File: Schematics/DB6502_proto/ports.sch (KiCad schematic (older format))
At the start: 12 parts, among them J1 System Bus, J2 Controls, J4 I/O Bus

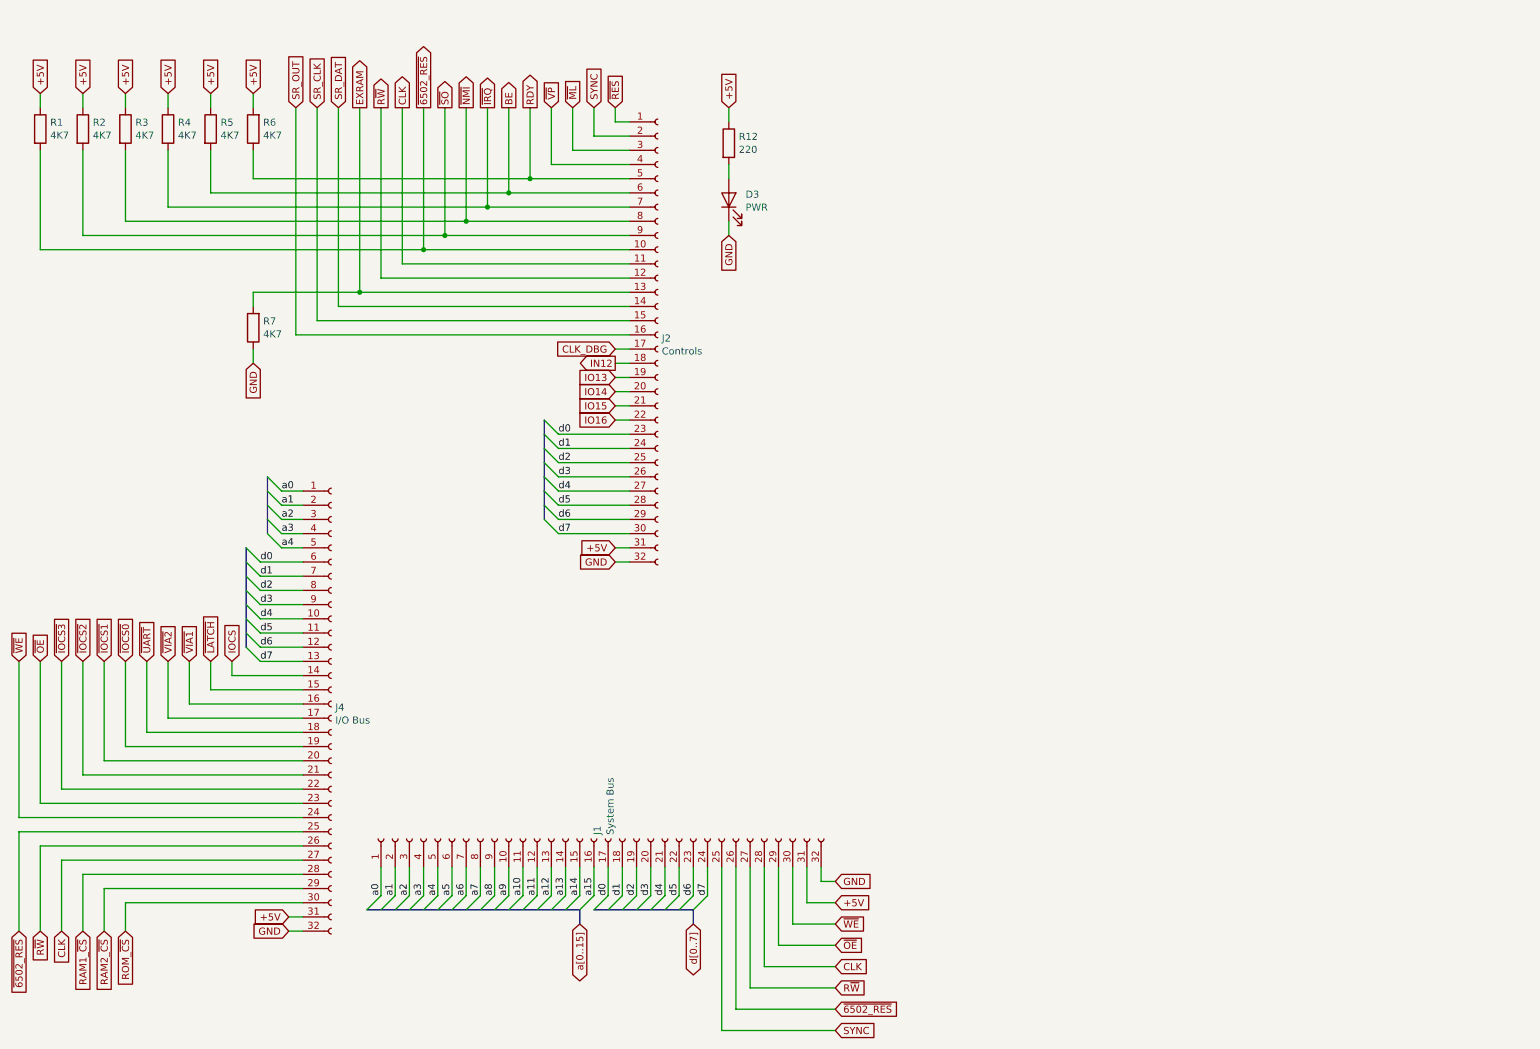
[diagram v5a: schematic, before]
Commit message: Implemented wait state generator, cleaned up schematic
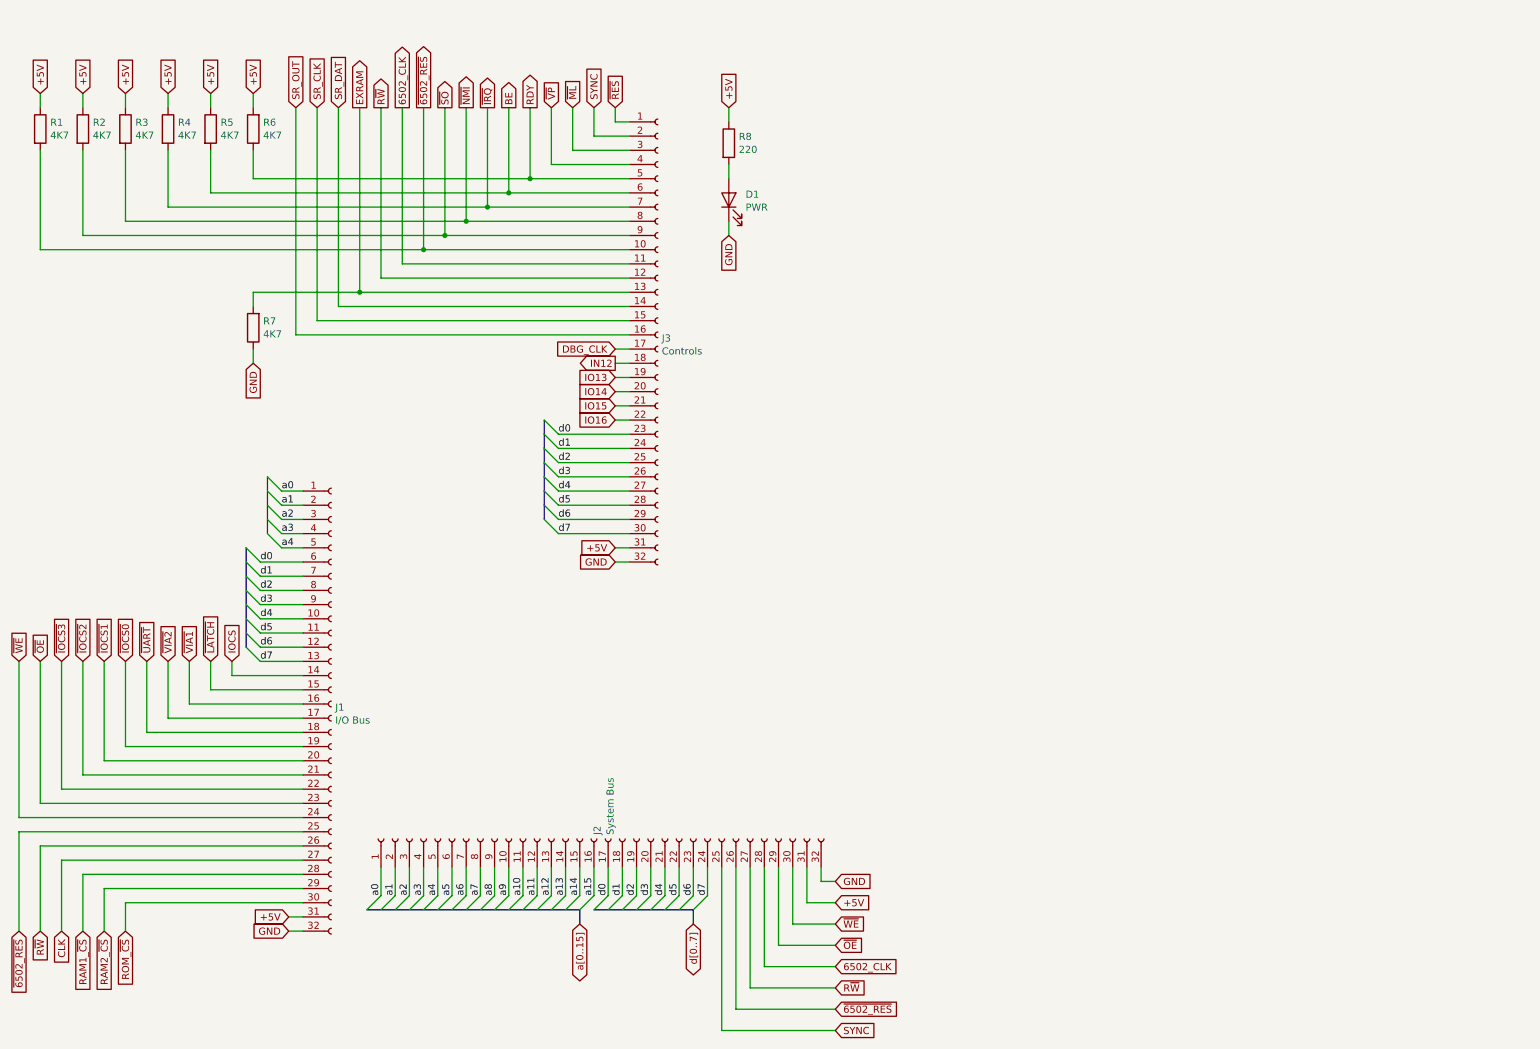
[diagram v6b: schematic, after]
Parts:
- renumbered D3 to D1, J4 to J1, J1 to J2, J2 to J3, R12 to R8
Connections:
- net CLK: no longer J2.28 (Pin_28), J3.11 (Pin_11)
- net CLK_DBG renamed DBG_CLK
- new net 6502_CLK: J2.28 (Pin_28), J3.11 (Pin_11)
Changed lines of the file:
@@
 $EndDescr
 $Comp
-L Connector:Conn_01x32_Female J1
+L Connector:Conn_01x32_Female J2
 U 1 1 6014BD0C
 P 4700 6200
-F 0 "J1" H 4728 6176 50  0000 L CNN
+F 0 "J2" H 4728 6176 50  0000 L CNN
 F 1 "System Bus" H 4728 6085 50  0000 L CNN
 F 2 "Connector_PinSocket_2.54mm:PinSocket_1x32_P2.54mm_Vertical" H 4700 6200 50  0001 C CNN
@@
 ~SO
 Text GLabel 3350 1050 1    50   Output ~ 0
-CLK
+6502_CLK
 Text GLabel 3200 1050 1    50   Output ~ 0
 R~W
@@
 	4700 1250 4950 1250
 $Comp
-L Connector:Conn_01x32_Female J2
+L Connector:Conn_01x32_Female J3
 U 1 1 60166003
 P 5150 2650
-F 0 "J2" H 5178 2626 50  0000 L CNN
+F 0 "J3" H 5178 2626 50  0000 L CNN
 F 1 "Controls" H 5178 2535 50  0000 L CNN
 F 2 "Connector_PinSocket_2.54mm:PinSocket_1x32_P2.54mm_Vertical" H 5150 2650 50  0001 C CNN
@@
 	3200 2250 4950 2250
 $Comp
-L Connector:Conn_01x32_Female J4
+L Connector:Conn_01x32_Female J1
 U 1 1 60200164
 P 2850 5250
-F 0 "J4" H 2878 5226 50  0000 L CNN
+F 0 "J1" H 2878 5226 50  0000 L CNN
 F 1 "I/O Bus" H 2878 5135 50  0000 L CNN
 F 2 "Connector_PinSocket_2.54mm:PinSocket_1x32_P2.54mm_Vertical" H 2850 5250 50  0001 C CNN
@@
 	2550 6850 2650 6850
 Text GLabel 6400 7100 2    50   Input ~ 0
-CLK
+6502_CLK
 Wire Wire Line
 	6400 7100 5900 7100
@@
 	5600 7550 5600 6400
 Text GLabel 4850 2750 0    50   Input ~ 0
-CLK_DBG
+DBG_CLK
 Wire Wire Line
 	4850 2750 4950 2750
@@
 	1400 6650 2650 6650
 $Comp
-L Device:R R12
+L Device:R R8
 U 1 1 60B17A68
 P 5650 1300
-F 0 "R12" H 5720 1346 50  0000 L CNN
+F 0 "R8" H 5720 1346 50  0000 L CNN
 F 1 "220" H 5720 1255 50  0000 L CNN
 F 2 "Resistor_THT:R_Axial_DIN0207_L6.3mm_D2.5mm_P10.16mm_Horizontal" V 5580 1300 50  0001 C CNN
@@
 $EndComp
 $Comp
-L Device:LED D3
+L Device:LED D1
 U 1 1 60B19002
 P 5650 1700
-F 0 "D3" V 5689 1582 50  0000 R CNN
+F 0 "D1" V 5689 1582 50  0000 R CNN
 F 1 "PWR" V 5598 1582 50  0000 R CNN
 F 2 "LED_THT:LED_D3.0mm" H 5650 1700 50  0001 C CNN

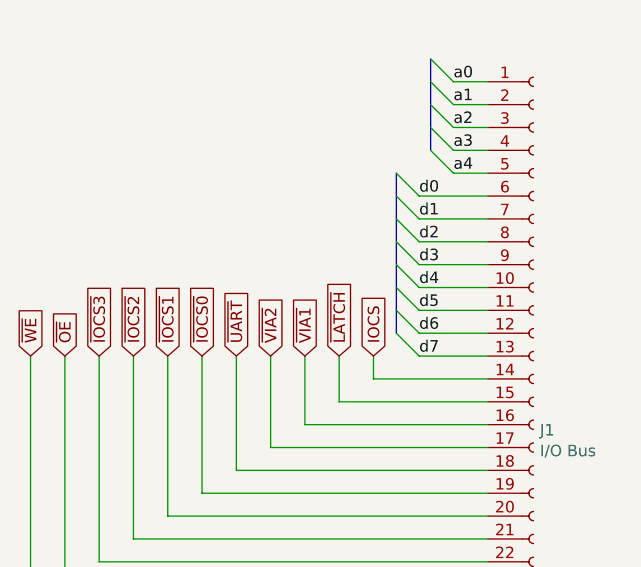
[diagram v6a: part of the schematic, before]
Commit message: Added I/O schematics page with DUART chip
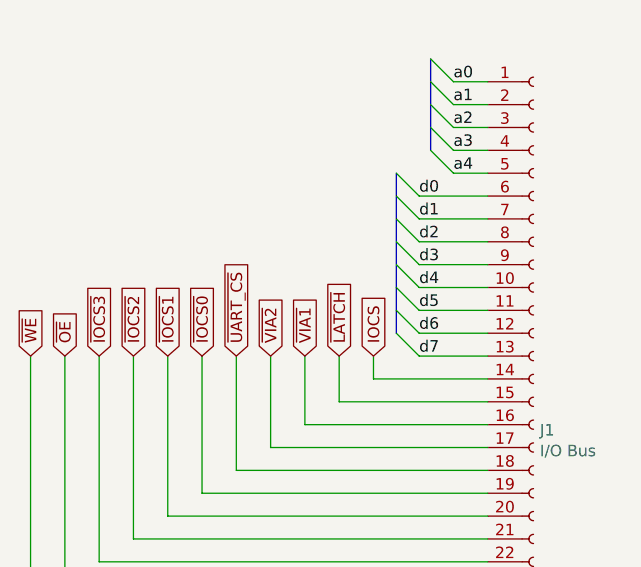
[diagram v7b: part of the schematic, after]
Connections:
- net ~UART renamed ~UART_CS
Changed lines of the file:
@@
 $Descr A4 11693 8268
 encoding utf-8
-Sheet 2 3
+Sheet 2 4
 Title "DB6502 Hobby Computer Version 2"
 Date "2020-10-13"
@@
 ~VIA2
 Text GLabel 1550 4950 1    50   Input ~ 0
-~UART
+~UART_CS
 Text GLabel 1400 4950 1    50   Input ~ 0
 ~IOCS0

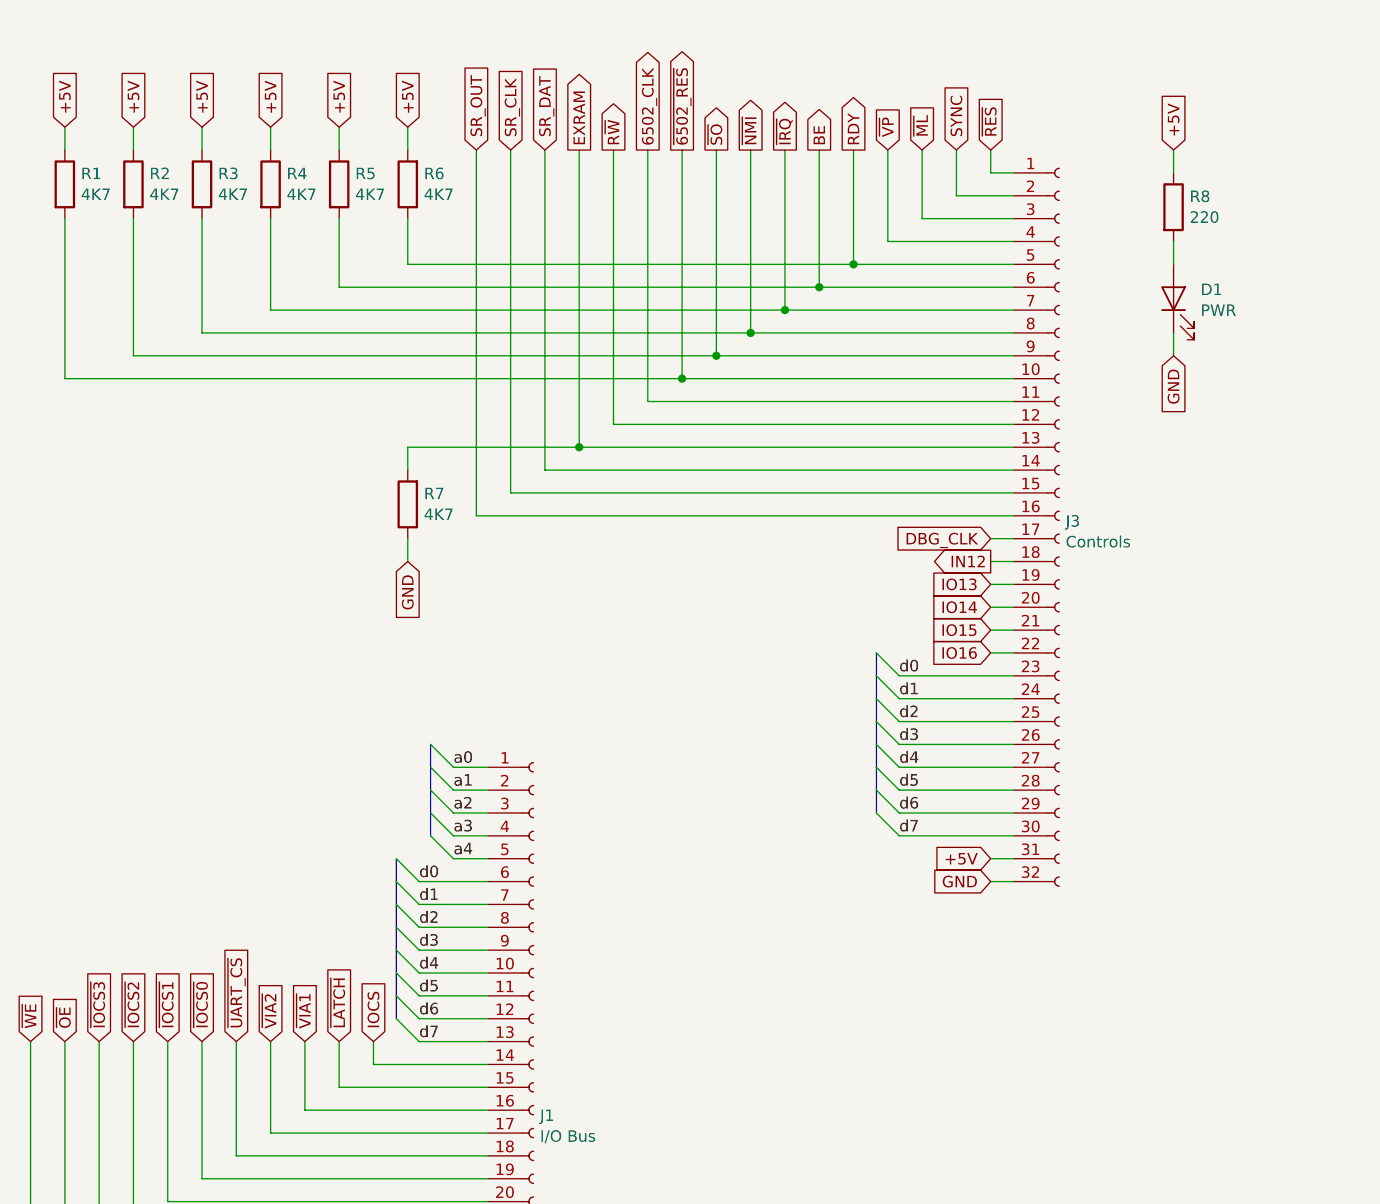
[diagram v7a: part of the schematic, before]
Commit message: Fixed issue with UART CEN during low clock, added IRQ gate
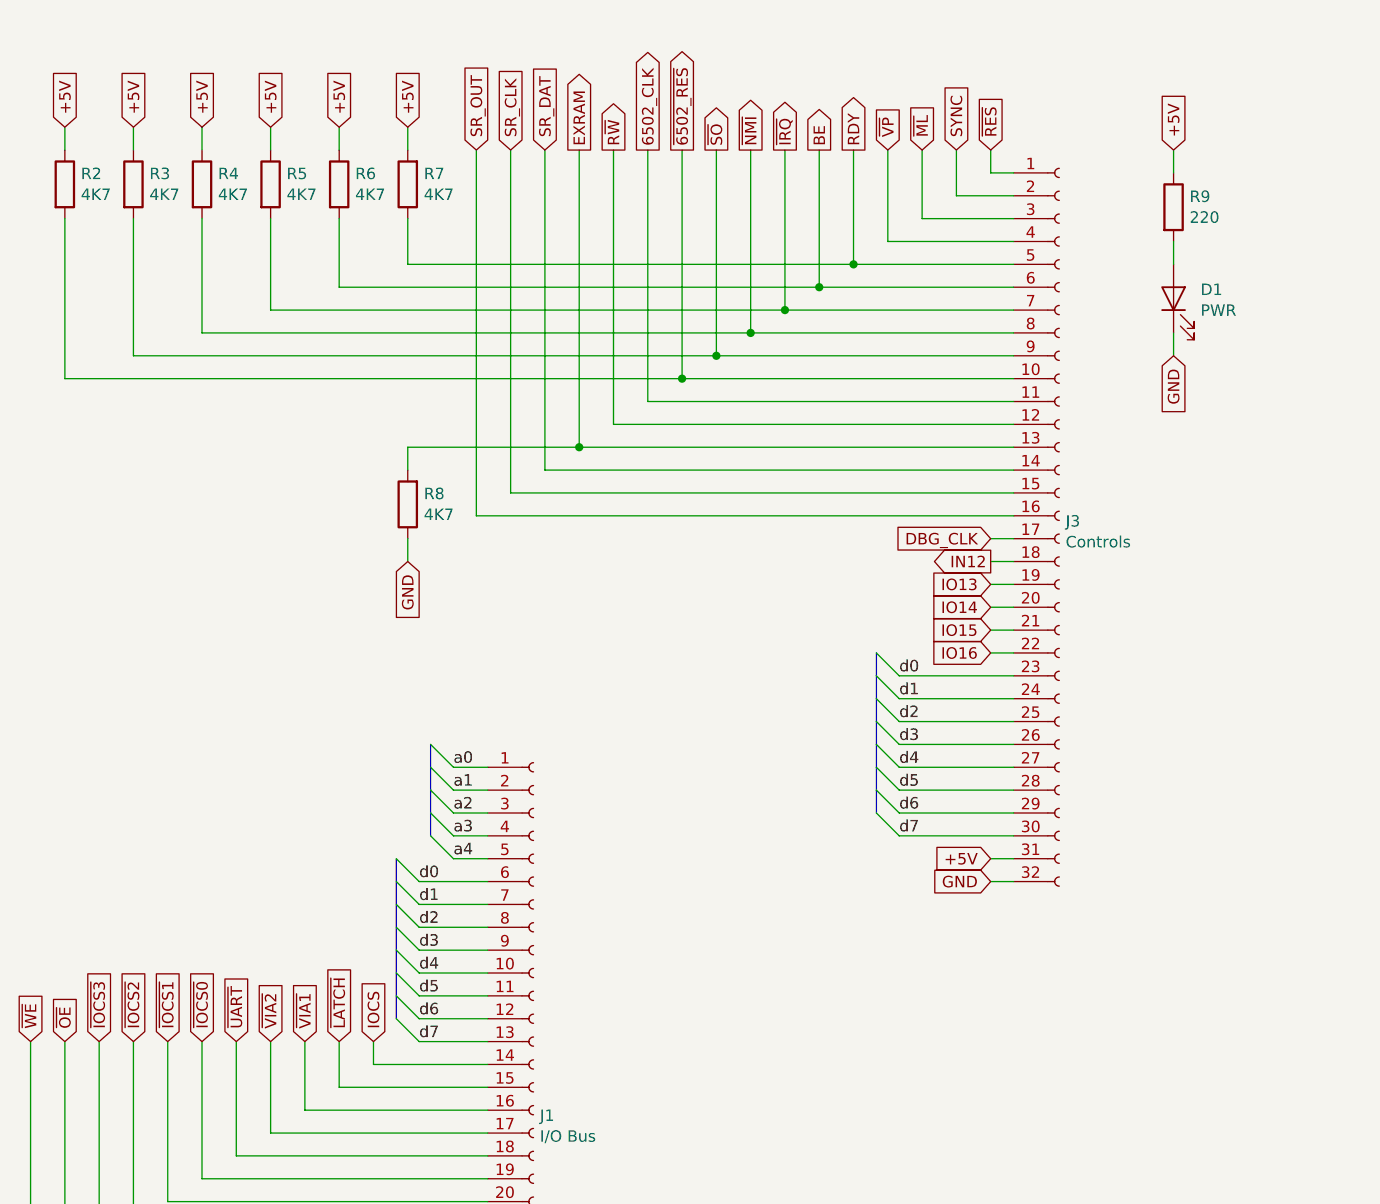
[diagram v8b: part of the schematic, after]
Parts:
- renumbered R1 to R2, R2 to R3, R3 to R4, R4 to R5, R5 to R6, R6 to R7, R7 to R8, R8 to R9
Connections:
- net ~UART_CS renamed ~UART
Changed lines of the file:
@@
 +5V
 $Comp
-L Device:R R6
+L Device:R R7
 U 1 1 6017257F
 P 2300 1200
-F 0 "R6" H 2230 1154 50  0000 R CNN
+F 0 "R7" H 2230 1154 50  0000 R CNN
 F 1 "4K7" H 2230 1245 50  0000 R CNN
 F 2 "Resistor_THT:R_Axial_DIN0207_L6.3mm_D2.5mm_P10.16mm_Horizontal" V 2230 1200 50  0001 C CNN
@@
 +5V
 $Comp
-L Device:R R5
+L Device:R R6
 U 1 1 6017DC7B
 P 2000 1200
-F 0 "R5" H 2070 1246 50  0000 L CNN
+F 0 "R6" H 2070 1246 50  0000 L CNN
 F 1 "4K7" H 2070 1155 50  0000 L CNN
 F 2 "Resistor_THT:R_Axial_DIN0207_L6.3mm_D2.5mm_P10.16mm_Horizontal" V 1930 1200 50  0001 C CNN
@@
 +5V
 $Comp
-L Device:R R4
+L Device:R R5
 U 1 1 601857FE
 P 1700 1200
-F 0 "R4" H 1770 1246 50  0000 L CNN
+F 0 "R5" H 1770 1246 50  0000 L CNN
 F 1 "4K7" H 1770 1155 50  0000 L CNN
 F 2 "Resistor_THT:R_Axial_DIN0207_L6.3mm_D2.5mm_P10.16mm_Horizontal" V 1630 1200 50  0001 C CNN
@@
 +5V
 $Comp
-L Device:R R3
+L Device:R R4
 U 1 1 601898AB
 P 1400 1200
-F 0 "R3" H 1470 1246 50  0000 L CNN
+F 0 "R4" H 1470 1246 50  0000 L CNN
 F 1 "4K7" H 1470 1155 50  0000 L CNN
 F 2 "Resistor_THT:R_Axial_DIN0207_L6.3mm_D2.5mm_P10.16mm_Horizontal" V 1330 1200 50  0001 C CNN
@@
 +5V
 $Comp
-L Device:R R2
+L Device:R R3
 U 1 1 601C227D
 P 1100 1200
-F 0 "R2" H 1170 1246 50  0000 L CNN
+F 0 "R3" H 1170 1246 50  0000 L CNN
 F 1 "4K7" H 1170 1155 50  0000 L CNN
 F 2 "Resistor_THT:R_Axial_DIN0207_L6.3mm_D2.5mm_P10.16mm_Horizontal" V 1030 1200 50  0001 C CNN
@@
 +5V
 $Comp
-L Device:R R1
+L Device:R R2
 U 1 1 601F1941
 P 800 1200
-F 0 "R1" H 870 1246 50  0000 L CNN
+F 0 "R2" H 870 1246 50  0000 L CNN
 F 1 "4K7" H 870 1155 50  0000 L CNN
 F 2 "Resistor_THT:R_Axial_DIN0207_L6.3mm_D2.5mm_P10.16mm_Horizontal" V 730 1200 50  0001 C CNN
@@
 ~VIA2
 Text GLabel 1550 4950 1    50   Input ~ 0
-~UART_CS
+~UART
 Text GLabel 1400 4950 1    50   Input ~ 0
 ~IOCS0
@@
 	2600 2650 4950 2650
 $Comp
-L Device:R R7
+L Device:R R8
 U 1 1 604F21BB
 P 2300 2600
-F 0 "R7" H 2230 2554 50  0000 R CNN
+F 0 "R8" H 2230 2554 50  0000 R CNN
 F 1 "4K7" H 2230 2645 50  0000 R CNN
 F 2 "Resistor_THT:R_Axial_DIN0207_L6.3mm_D2.5mm_P10.16mm_Horizontal" V 2230 2600 50  0001 C CNN
@@
 	1400 6650 2650 6650
 $Comp
-L Device:R R8
+L Device:R R9
 U 1 1 60B17A68
 P 5650 1300
-F 0 "R8" H 5720 1346 50  0000 L CNN
+F 0 "R9" H 5720 1346 50  0000 L CNN
 F 1 "220" H 5720 1255 50  0000 L CNN
 F 2 "Resistor_THT:R_Axial_DIN0207_L6.3mm_D2.5mm_P10.16mm_Horizontal" V 5580 1300 50  0001 C CNN
